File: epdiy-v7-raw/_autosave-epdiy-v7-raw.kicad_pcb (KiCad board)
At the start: 4 copper layers, 128.4 x 74.9 mm, 110 parts, among them CN1 WP27D-S050VA3-R15000, IC1 MPU-6500, J1 USB_C_Receptacle_USB2.0, J2 EXTENSION_HEADER, J3 SIGNALS_HEADER, J5 CONN_BAT, J7 ESP_HDR, Q1 AO3401A, SW1 TC-0522C-1.7-160G, SW2 TC-0522C-1.7-160G, U1 RT9080-33GJ5, U10 ED060XC5, U11 TP4056, U3 TPS651851RSLR, U4 USBLC6-2P6, U8 ESP32-S3-WROOM-1, Y1 RV-3032-C7

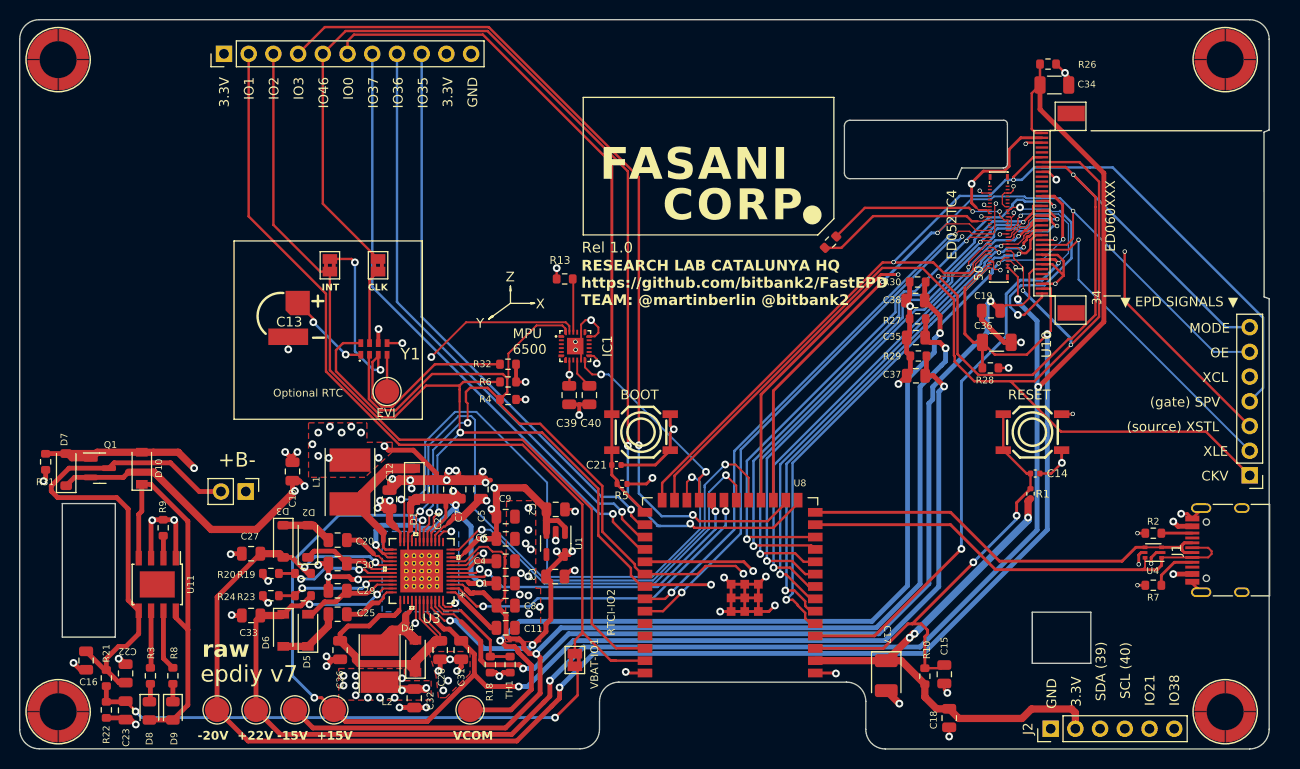
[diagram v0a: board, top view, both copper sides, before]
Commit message: Updated and NUT SMD corrected (KiCad 8)
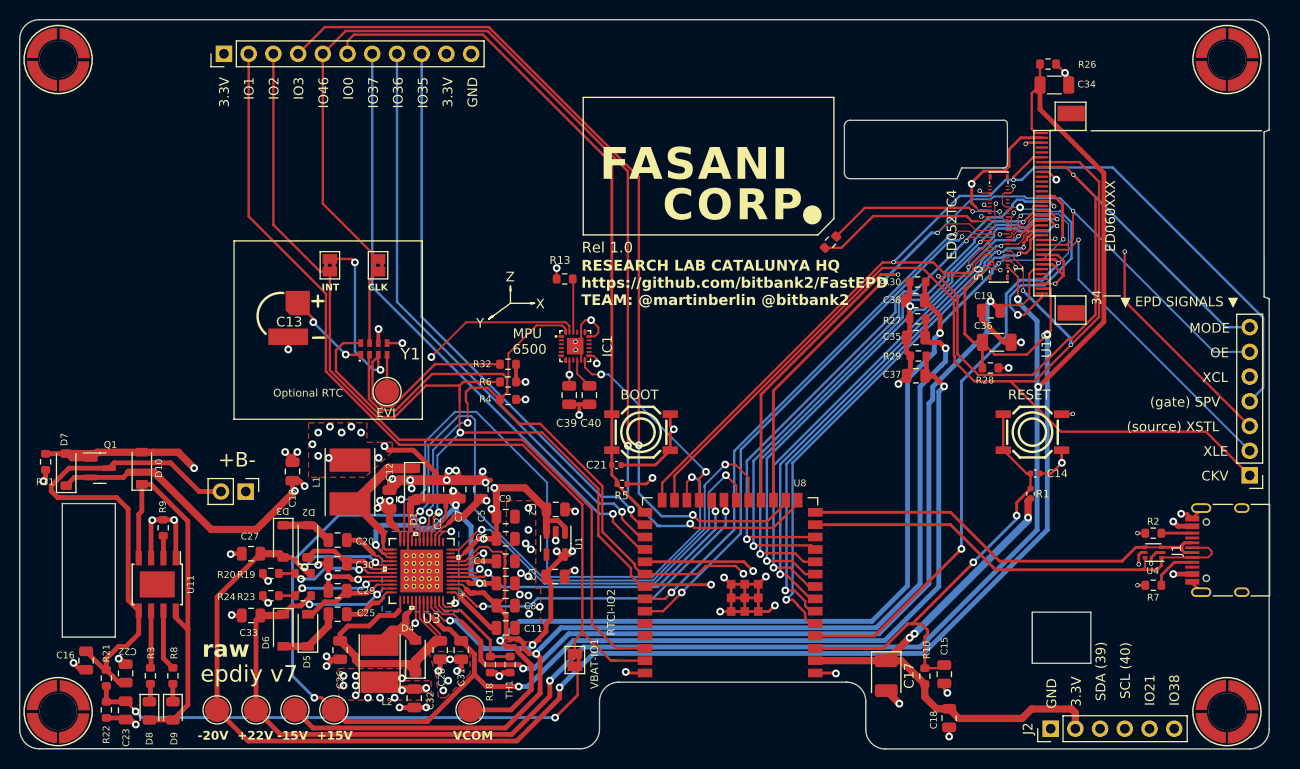
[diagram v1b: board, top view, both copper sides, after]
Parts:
- moved H2 0.18 mm to (182.1, 51.8)
- moved H4 0.18 mm to (182.1, 118.8)
